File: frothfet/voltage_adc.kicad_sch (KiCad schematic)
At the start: 4 parts, among them U23 ADS1015IDGS

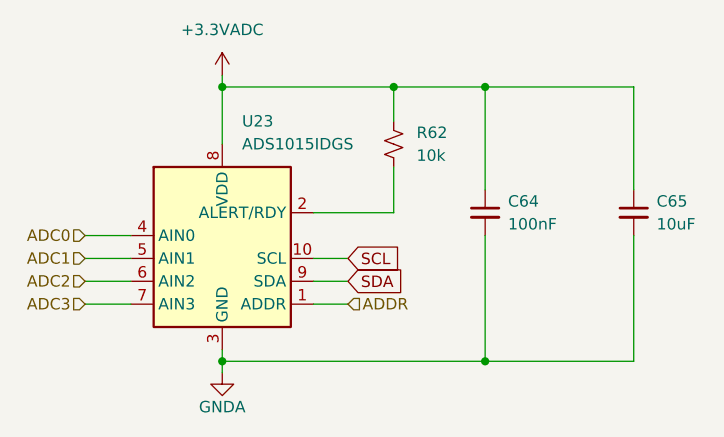
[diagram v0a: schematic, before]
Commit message: added extra adc control lines
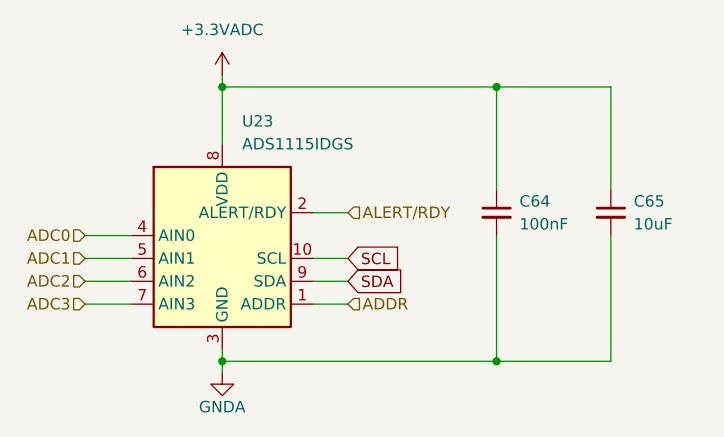
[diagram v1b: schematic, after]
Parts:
- removed R62: 10k, Resistor_SMD:R_0805_2012Metric_Pad1.20x1.40mm_HandSolder, symbol Device:R_Small_US
- U23: value ADS1015IDGS -> ADS1115IDGS; LCSC C193969 -> (none)
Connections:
- net ALERT/RDY: now reaches U23.2 (ALERT/RDY)
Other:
- moved on the sheet: C64, C65
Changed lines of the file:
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@@
-	)
-	(junction
-		(at 157.48 77.47)
-		(diameter 0)
-		(color 0 0 0 0)
 	)
 	(junction
@@
 	)
 	(junction
-		(at 167.64 77.47)
+		(at 168.91 77.47)
 		(diameter 0)
 		(color 0 0 0 0)
 	)
 	(junction
-		(at 167.64 107.95)
+		(at 168.91 107.95)
 		(diameter 0)
 		(color 0 0 0 0)
@@
 	(wire
 		(pts
-			(xy 184.15 93.98) (xy 184.15 107.95)
-		)
-		(stroke
-			(width 0)
-			(type default)
-		)
-	)
-	(wire
-		(pts
-			(xy 167.64 77.47) (xy 184.15 77.47)
+			(xy 181.61 93.98) (xy 181.61 107.95)
+		)
+		(stroke
+			(width 0)
+			(type default)
+		)
+	)
+	(wire
+		(pts
+			(xy 168.91 77.47) (xy 181.61 77.47)
 		)
 		(stroke
@@
 	(wire
 		(pts
-			(xy 157.48 91.44) (xy 157.48 86.36)
-		)
-		(stroke
-			(width 0)
-			(type default)
-		)
-	)
-	(wire
-		(pts
 			(xy 138.43 106.68) (xy 138.43 107.95)
 		)
@@
 	(wire
 		(pts
-			(xy 138.43 77.47) (xy 157.48 77.47)
+			(xy 138.43 77.47) (xy 168.91 77.47)
 		)
 		(stroke
@@
 	(wire
 		(pts
-			(xy 184.15 77.47) (xy 184.15 88.9)
+			(xy 181.61 77.47) (xy 181.61 88.9)
 		)
 		(stroke
@@
 	(wire
 		(pts
-			(xy 184.15 107.95) (xy 167.64 107.95)
-		)
-		(stroke
-			(width 0)
-			(type default)
-		)
-	)
-	(wire
-		(pts
-			(xy 148.59 91.44) (xy 157.48 91.44)
-		)
-		(stroke
-			(width 0)
-			(type default)
-		)
-	)
-	(wire
-		(pts
-			(xy 167.64 93.98) (xy 167.64 107.95)
-		)
-		(stroke
-			(width 0)
-			(type default)
-		)
-	)
-	(wire
-		(pts
-			(xy 167.64 77.47) (xy 167.64 88.9)
+			(xy 181.61 107.95) (xy 168.91 107.95)
+		)
+		(stroke
+			(width 0)
+			(type default)
+		)
+	)
+	(wire
+		(pts
+			(xy 148.59 91.44) (xy 152.4 91.44)
+		)
+		(stroke
+			(width 0)
+			(type default)
+		)
+	)
+	(wire
+		(pts
+			(xy 168.91 93.98) (xy 168.91 107.95)
+		)
+		(stroke
+			(width 0)
+			(type default)
+		)
+	)
+	(wire
+		(pts
+			(xy 168.91 77.47) (xy 168.91 88.9)
 		)
 		(stroke
@@
 	(wire
 		(pts
-			(xy 157.48 77.47) (xy 157.48 81.28)
-		)
-		(stroke
-			(width 0)
-			(type default)
-		)
-	)
-	(wire
-		(pts
-			(xy 157.48 77.47) (xy 167.64 77.47)
-		)
-		(stroke
-			(width 0)
-			(type default)
-		)
-	)
-	(wire
-		(pts
 			(xy 138.43 76.2) (xy 138.43 77.47)
 		)
@@
 	(wire
 		(pts
-			(xy 167.64 107.95) (xy 138.43 107.95)
+			(xy 168.91 107.95) (xy 138.43 107.95)
 		)
 		(stroke
@@
 		)
 	)
+	(hierarchical_label "ALERT{slash}RDY"
+		(shape input)
+		(at 152.4 91.44 0)
+		(fields_autoplaced yes)
+		(effects
+			(font
+				(size 1.27 1.27)
+			)
+			(justify left)
+		)
+	)
 	(hierarchical_label "ADC2"
 		(shape input)
@@
 	(symbol
 		(lib_id "Device:C_Small")
-		(at 167.64 91.44 0)
+		(at 168.91 91.44 0)
 		(unit 1)
 		(exclude_from_sim no)
@@
 		(dnp no)
 		(property "Reference" "C64"
-			(at 170.18 90.1763 0)
+			(at 171.45 90.1763 0)
 			(effects
 				(font
@@
 		)
 		(property "Value" "100nF"
-			(at 170.18 92.7163 0)
+			(at 171.45 92.7163 0)
 			(effects
 				(font
@@
 		)
 		(property "Footprint" "Capacitor_SMD:C_0805_2012Metric_Pad1.18x1.45mm_HandSolder"
-			(at 167.64 91.44 0)
+			(at 168.91 91.44 0)
 			(effects
 				(font
@@
 		)
 		(property "Datasheet" "~"
-			(at 167.64 91.44 0)
+			(at 168.91 91.44 0)
 			(effects
 				(font
@@
 		)
 		(property "Description" ""
-			(at 167.64 91.44 0)
+			(at 168.91 91.44 0)
 			(effects
 				(font
@@
 		)
 		(property "Mouser" ""
-			(at 167.64 91.44 0)
+			(at 168.91 91.44 0)
 			(effects
 				(font
@@
 		)
 		(property "LCSC" "C49678"
-			(at 167.64 91.44 0)
+			(at 168.91 91.44 0)
 			(effects
 				(font
@@
 		)
 		(property "ALT" ""
-			(at 167.64 91.44 0)
+			(at 168.91 91.44 0)
 			(effects
 				(font
@@
 			)
 		)
-		(property "Value" "ADS1015IDGS"
+		(property "Value" "ADS1115IDGS"
 			(at 140.6241 83.82 0)
 			(effects
@@
 			)
 		)
-		(property "LCSC" "C193969"
+		(property "LCSC" ""
 			(at 138.43 96.52 0)
 			(effects
@@
 	(symbol
 		(lib_id "Device:C_Small")
-		(at 184.15 91.44 0)
+		(at 181.61 91.44 0)
 		(unit 1)
 		(exclude_from_sim no)
@@
 		(dnp no)
 		(property "Reference" "C65"
-			(at 186.69 90.1763 0)
+			(at 184.15 90.1763 0)
 			(effects
 				(font
@@
 		)
 		(property "Value" "10uF"
-			(at 186.69 92.7163 0)
+			(at 184.15 92.7163 0)
 			(effects
 				(font
@@
 		)
 		(property "Footprint" "Capacitor_SMD:C_0805_2012Metric_Pad1.18x1.45mm_HandSolder"
-			(at 184.15 91.44 0)
+			(at 181.61 91.44 0)
 			(effects
 				(font
@@
 		)
 		(property "Datasheet" "~"
-			(at 184.15 91.44 0)
+			(at 181.61 91.44 0)
 			(effects
 				(font
@@
 		)
 		(property "Description" ""
-			(at 184.15 91.44 0)
+			(at 181.61 91.44 0)
 			(effects
 				(font
@@
 		)
 		(property "Vendor" ""
-			(at 184.15 91.44 0)
+			(at 181.61 91.44 0)
 			(effects
 				(font
@@
 		)
 		(property "LCSC" "C1952580"
-			(at 184.15 91.44 0)
+			(at 181.61 91.44 0)
 			(effects
 				(font
@@
 		)
 		(property "ALT" ""
-			(at 184.15 91.44 0)
+			(at 181.61 91.44 0)
 			(effects
 				(font
@@
 					(unit 1)
 				)
-			)
-		)
-	)
-	(symbol
-		(lib_id "Device:R_Small_US")
-		(at 157.48 83.82 180)
-		(unit 1)
-		(exclude_from_sim no)
-		(in_bom yes)
-		(on_board yes)
-		(dnp no)
-		(fields_autoplaced yes)
-		(property "Reference" "R62"
-			(at 160.02 82.55 0)
-			(effects
-				(font
-					(size 1.27 1.27)
-				)
-				(justify right)
-			)
-		)
-		(property "Value" "10k"
-			(at 160.02 85.09 0)
-			(effects
-				(font
-					(size 1.27 1.27)
-				)
-				(justify right)
-			)
-		)
-		(property "Footprint" "Resistor_SMD:R_0805_2012Metric_Pad1.20x1.40mm_HandSolder"
-			(at 157.48 83.82 0)
-			(effects
-				(font
-					(size 1.27 1.27)
-				)
-				(hide yes)
-			)
-		)
-		(property "Datasheet" "~"
-			(at 157.48 83.82 0)
-			(effects
-				(font
-					(size 1.27 1.27)
-				)
-				(hide yes)
-			)
-		)
-		(property "Description" ""
-			(at 157.48 83.82 0)
-			(effects
-				(font
-					(size 1.27 1.27)
-				)
-				(hide yes)
-			)
-		)
-		(property "LCSC" "C84376"
-			(at 157.48 83.82 0)
-			(effects
-				(font
-					(size 1.27 1.27)
-				)
-				(hide yes)
-			)
-		)
-		(property "ALT" ""
-			(at 157.48 83.82 0)
-			(effects
-				(font
-					(size 1.27 1.27)
-				)
-				(hide yes)
-			)
-		)
-		(pin "1"
-		)
-		(pin "2"
-		)
-		(instances
-			(project "8ch-mosfet"
-				(path "/c83c6236-96e9-46ad-9d7a-9e2efa4a7966/a6260305-24e3-4714-b441-a7a157c17bd9"
-					(reference "R62")
-					(unit 1)
-				)
-				(path "/c83c6236-96e9-46ad-9d7a-9e2efa4a7966/bb9dea8b-8412-49bc-950d-dce57727bcd2"
-					(reference "R61")
-					(unit 1)
-				)
